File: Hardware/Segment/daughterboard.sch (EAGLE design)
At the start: 170 parts, among them IC1 PBQ79656PAPTQ1, IC2 PBQ79656PAPTQ1, T1 PBHV8115X, 115, T2 PBHV8115X, 115

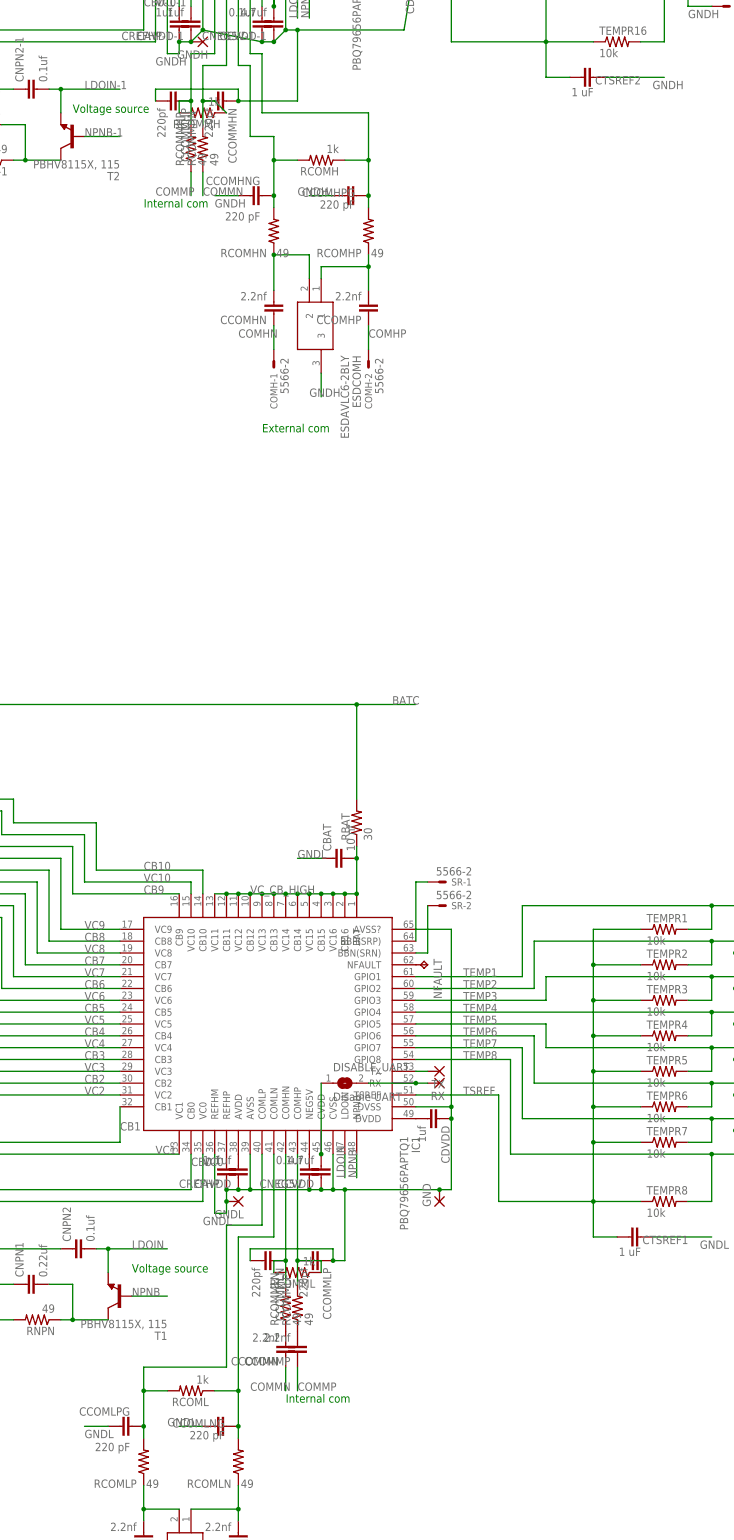
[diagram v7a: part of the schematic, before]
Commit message: All components on top of daughterboard
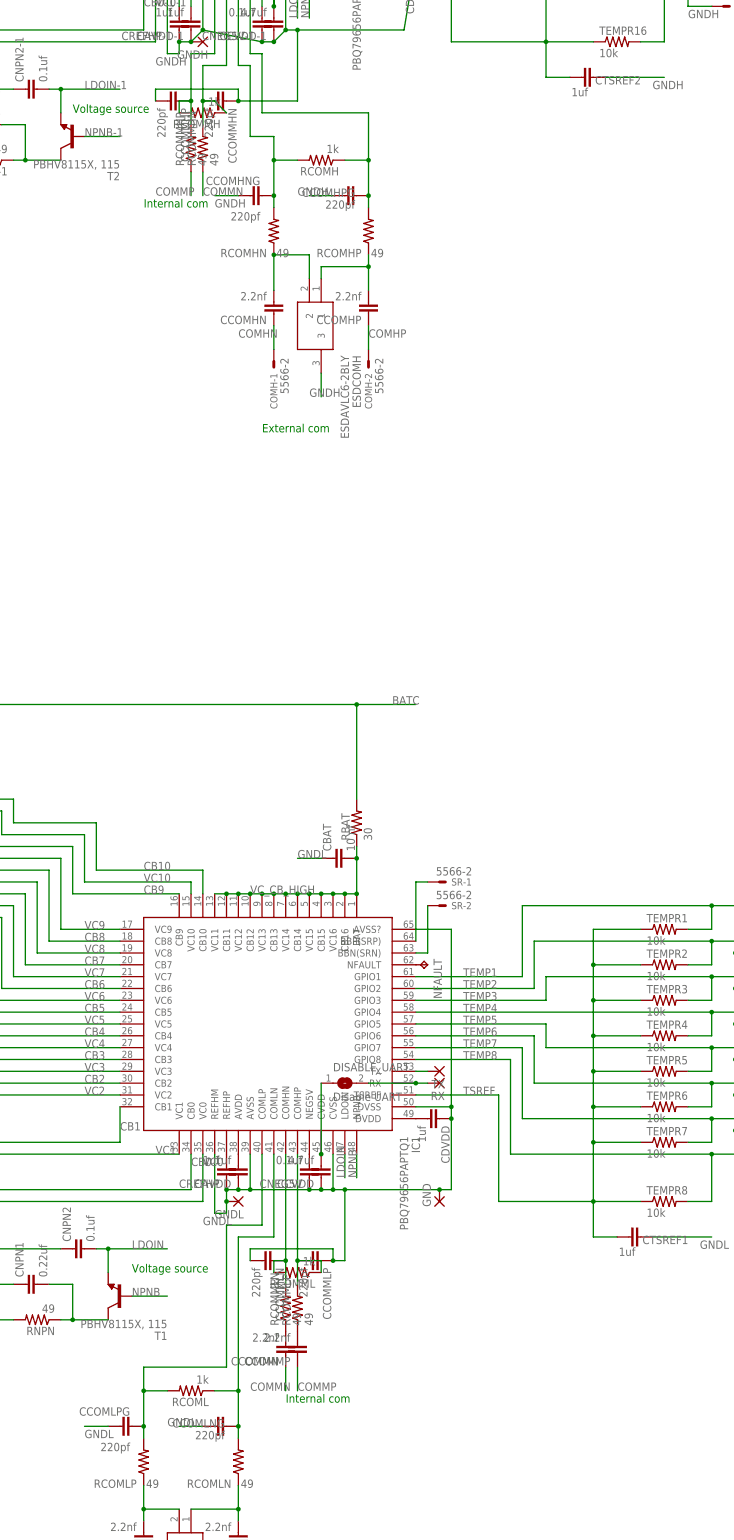
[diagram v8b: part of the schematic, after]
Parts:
- CCOMHNG, CCOMHPG, CCOMLNG, CCOMLPG: value 220 pF -> 220pf
- CTSREF1, CTSREF2: value 1 uF -> 1uf
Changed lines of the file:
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@@
 <part name="TEMPL" library="con-molex" library_urn="urn:adsk.eagle:library:165" deviceset="5566-16" device="" package3d_urn="urn:adsk.eagle:package:8078576/1"/>
 <part name="TEMPR8" library="rcl" library_urn="urn:adsk.eagle:library:334" deviceset="R-US_" device="R0603" package3d_urn="urn:adsk.eagle:package:23555/3" value="10k"/>
-<part name="CTSREF1" library="rcl" library_urn="urn:adsk.eagle:library:334" deviceset="C-EU" device="C0603" package3d_urn="urn:adsk.eagle:package:23616/2" value="1 uF"/>
+<part name="CTSREF1" library="rcl" library_urn="urn:adsk.eagle:library:334" deviceset="C-EU" device="C0603" package3d_urn="urn:adsk.eagle:package:23616/2" value="1uf"/>
 <part name="TEMPR7" library="rcl" library_urn="urn:adsk.eagle:library:334" deviceset="R-US_" device="R0603" package3d_urn="urn:adsk.eagle:package:23555/3" value="10k"/>
 <part name="TEMPR6" library="rcl" library_urn="urn:adsk.eagle:library:334" deviceset="R-US_" device="R0603" package3d_urn="urn:adsk.eagle:package:23555/3" value="10k"/>
@@
 <part name="T1" library="transistor" library_urn="urn:adsk.eagle:library:402" deviceset="*-NPN-" device="SOT89-BCE" package3d_urn="urn:adsk.eagle:package:29925/3" technology="BC868" value="PBHV8115X, 115"/>
 <part name="RCOML" library="rcl" library_urn="urn:adsk.eagle:library:334" deviceset="R-US_" device="R0603" package3d_urn="urn:adsk.eagle:package:23555/3" value="1k"/>
-<part name="CCOMLNG" library="rcl" library_urn="urn:adsk.eagle:library:334" deviceset="C-EU" device="C0603" package3d_urn="urn:adsk.eagle:package:23616/2" value="220 pF"/>
+<part name="CCOMLNG" library="rcl" library_urn="urn:adsk.eagle:library:334" deviceset="C-EU" device="C0603" package3d_urn="urn:adsk.eagle:package:23616/2" value="220pf"/>
 <part name="RCOMLN" library="rcl" library_urn="urn:adsk.eagle:library:334" deviceset="R-US_" device="R0603" package3d_urn="urn:adsk.eagle:package:23555/3" value="49"/>
 <part name="RCOMLP" library="rcl" library_urn="urn:adsk.eagle:library:334" deviceset="R-US_" device="R0603" package3d_urn="urn:adsk.eagle:package:23555/3" value="49"/>
 <part name="CCOMLN" library="rcl" library_urn="urn:adsk.eagle:library:334" deviceset="C-EU" device="C0603" package3d_urn="urn:adsk.eagle:package:23616/2" value="2.2nf"/>
 <part name="CCOMLP" library="rcl" library_urn="urn:adsk.eagle:library:334" deviceset="C-EU" device="C0603" package3d_urn="urn:adsk.eagle:package:23616/2" value="2.2nf"/>
-<part name="CCOMLPG" library="rcl" library_urn="urn:adsk.eagle:library:334" deviceset="C-EU" device="C0603" package3d_urn="urn:adsk.eagle:package:23616/2" value="220 pF"/>
+<part name="CCOMLPG" library="rcl" library_urn="urn:adsk.eagle:library:334" deviceset="C-EU" device="C0603" package3d_urn="urn:adsk.eagle:package:23616/2" value="220pf"/>
 <part name="ESDCOML" library="ESDAVLC6-2BLY" deviceset="ESDAVLC6-2BLY" device=""/>
 <part name="COML" library="con-molex" library_urn="urn:adsk.eagle:library:165" deviceset="5566-2" device="" package3d_urn="urn:adsk.eagle:package:8078583/1"/>
@@
 <part name="TEMPH" library="con-molex" library_urn="urn:adsk.eagle:library:165" deviceset="5566-16" device="" package3d_urn="urn:adsk.eagle:package:8078576/1"/>
 <part name="TEMPR16" library="rcl" library_urn="urn:adsk.eagle:library:334" deviceset="R-US_" device="R0603" package3d_urn="urn:adsk.eagle:package:23555/3" value="10k"/>
-<part name="CTSREF2" library="rcl" library_urn="urn:adsk.eagle:library:334" deviceset="C-EU" device="C0603" package3d_urn="urn:adsk.eagle:package:23616/2" value="1 uF"/>
+<part name="CTSREF2" library="rcl" library_urn="urn:adsk.eagle:library:334" deviceset="C-EU" device="C0603" package3d_urn="urn:adsk.eagle:package:23616/2" value="1uf"/>
 <part name="TEMPR15" library="rcl" library_urn="urn:adsk.eagle:library:334" deviceset="R-US_" device="R0603" package3d_urn="urn:adsk.eagle:package:23555/3" value="10k"/>
 <part name="TEMPR14" library="rcl" library_urn="urn:adsk.eagle:library:334" deviceset="R-US_" device="R0603" package3d_urn="urn:adsk.eagle:package:23555/3" value="10k"/>
@@
 <part name="T2" library="transistor" library_urn="urn:adsk.eagle:library:402" deviceset="*-NPN-" device="SOT89-BCE" package3d_urn="urn:adsk.eagle:package:29925/3" technology="BC868" value="PBHV8115X, 115"/>
 <part name="RCOMH" library="rcl" library_urn="urn:adsk.eagle:library:334" deviceset="R-US_" device="R0603" package3d_urn="urn:adsk.eagle:package:23555/3" value="1k"/>
-<part name="CCOMHPG" library="rcl" library_urn="urn:adsk.eagle:library:334" deviceset="C-EU" device="C0603" package3d_urn="urn:adsk.eagle:package:23616/2" value="220 pF"/>
+<part name="CCOMHPG" library="rcl" library_urn="urn:adsk.eagle:library:334" deviceset="C-EU" device="C0603" package3d_urn="urn:adsk.eagle:package:23616/2" value="220pf"/>
 <part name="RCOMHP" library="rcl" library_urn="urn:adsk.eagle:library:334" deviceset="R-US_" device="R0603" package3d_urn="urn:adsk.eagle:package:23555/3" value="49"/>
 <part name="RCOMHN" library="rcl" library_urn="urn:adsk.eagle:library:334" deviceset="R-US_" device="R0603" package3d_urn="urn:adsk.eagle:package:23555/3" value="49"/>
 <part name="CCOMHP" library="rcl" library_urn="urn:adsk.eagle:library:334" deviceset="C-EU" device="C0603" package3d_urn="urn:adsk.eagle:package:23616/2" value="2.2nf"/>
 <part name="CCOMHN" library="rcl" library_urn="urn:adsk.eagle:library:334" deviceset="C-EU" device="C0603" package3d_urn="urn:adsk.eagle:package:23616/2" value="2.2nf"/>
-<part name="CCOMHNG" library="rcl" library_urn="urn:adsk.eagle:library:334" deviceset="C-EU" device="C0603" package3d_urn="urn:adsk.eagle:package:23616/2" value="220 pF"/>
+<part name="CCOMHNG" library="rcl" library_urn="urn:adsk.eagle:library:334" deviceset="C-EU" device="C0603" package3d_urn="urn:adsk.eagle:package:23616/2" value="220pf"/>
 <part name="ESDCOMH" library="ESDAVLC6-2BLY" deviceset="ESDAVLC6-2BLY" device=""/>
 <part name="COMH" library="con-molex" library_urn="urn:adsk.eagle:library:165" deviceset="5566-2" device="" package3d_urn="urn:adsk.eagle:package:8078583/1"/>
